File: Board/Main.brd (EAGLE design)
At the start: 40.6 x 45.7 mm, 9 parts, among them M1 LB1909MC, M2 LB1909MC

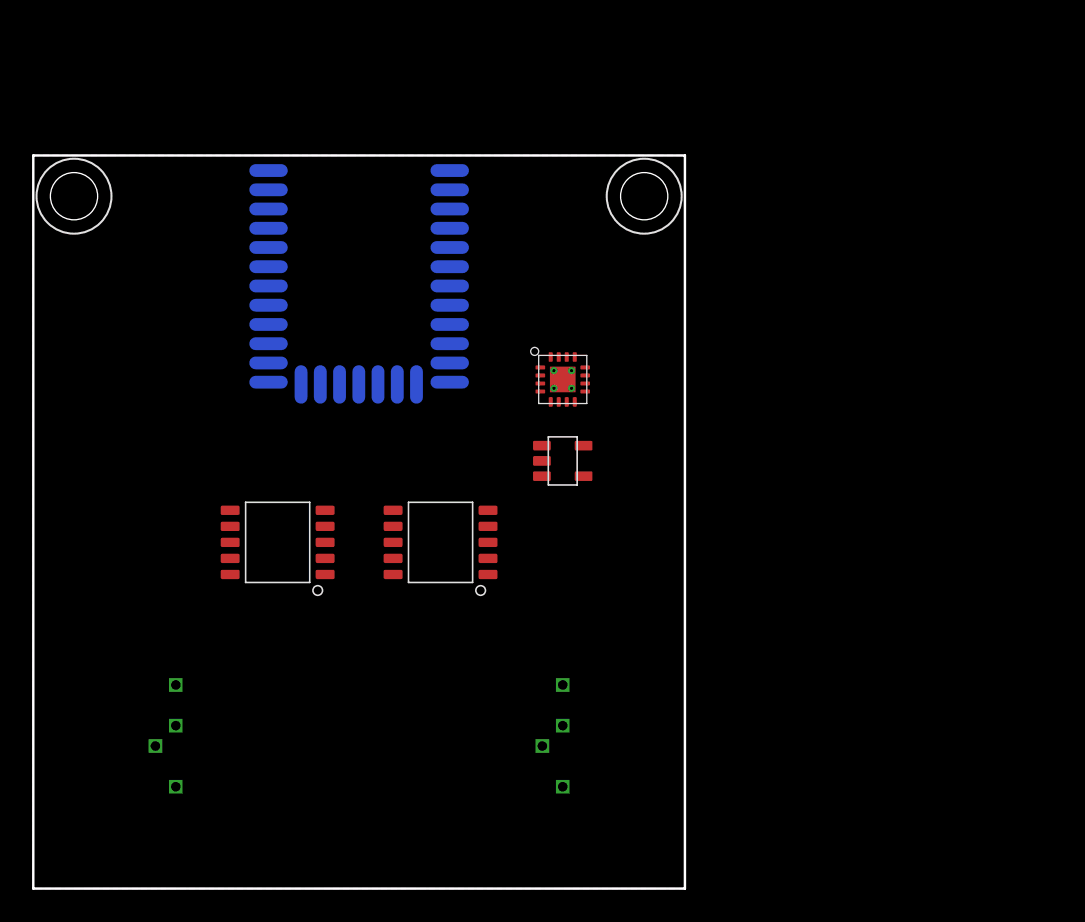
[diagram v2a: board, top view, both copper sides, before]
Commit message: Add USB connector
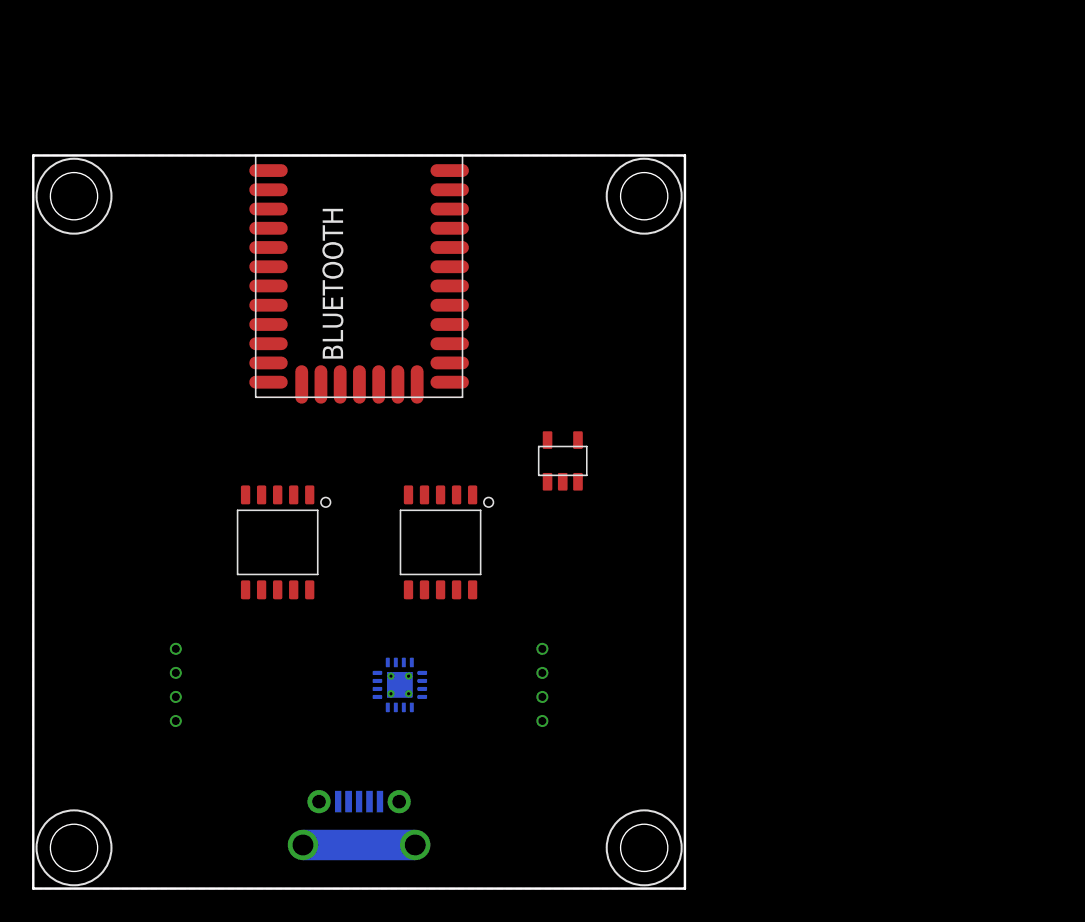
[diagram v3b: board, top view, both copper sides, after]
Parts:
- added LI-PO: 500mAh, Hardware:BATTERY
- added U$5, U$6: (no value), Hardware:#4_SCREW
- added USB: USB, Components:USB
- moved CHARGER 21.6 mm to (2.54, -10.2), flipped to the bottom, turned to 90 degrees
- moved U$3 2.84 mm to (11.4, -10.2), flipped to the bottom
- moved U$4 2.54 mm to (-11.4, -10.2), flipped to the bottom
- flipped BLUETOOTH to the top
- turned M1 to 270 degrees
- turned M2 to 270 degrees
- turned REGULATOR to 90 degrees
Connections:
- net +5V0: now also USB.1
- net GND: now also USB.5, USB.GND@0, USB.GND@1, USB.GND@2, USB.GND@3
- net N$2: now also U$4.B2; no longer U$4.P$2
- net N$3: now also U$3.B2; no longer U$3.P$2
- net N$4: now also U$3.B1; no longer U$3.P$1
- net N$5: now also U$4.B1; no longer U$4.P$1
- net N$6: now also U$4.A1; no longer U$4.P$3
- net N$7: now also U$4.A2; no longer U$4.P$4
- net N$8: now also U$3.A1; no longer U$3.P$3
- net N$9: now also U$3.A2; no longer U$3.P$4
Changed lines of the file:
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@@
 </autorouter>
 <elements>
-<element name="CHARGER" library="Main Components" package="VQFN-16" value="BQ24075" x="12.7" y="8.89" smashed="yes">
-<attribute name="VALUE" value="BQ24075" x="12.7" y="8.89" size="1.778" layer="27" display="off"/>
+<element name="CHARGER" library="Main Components" package="VQFN-16" value="BQ24075" x="2.54" y="-10.16" smashed="yes" rot="MR90">
+<attribute name="VALUE" value="BQ24075" x="2.54" y="-10.16" size="1.778" layer="28" rot="MR90" display="off"/>
 </element>
-<element name="BLUETOOTH" library="Main Components" package="BGM111" value="BGM111" x="0" y="22.86" smashed="yes" rot="MR0">
-<attribute name="NAME" x="1" y="14.86" size="1.27" layer="26" font="vector" rot="MR90" align="bottom-center"/>
-<attribute name="VALUE" x="-2" y="14.86" size="1.27" layer="28" font="vector" rot="MR90" align="bottom-center"/>
+<element name="BLUETOOTH" library="Main Components" package="BGM111" value="BGM111" x="0" y="22.86" smashed="yes">
+<attribute name="NAME" x="-1" y="14.86" size="1.27" layer="25" font="vector" rot="R90" align="bottom-center"/>
+<attribute name="VALUE" x="2" y="14.86" size="1.27" layer="27" font="vector" rot="R90" align="bottom-center"/>
 </element>
 <element name="U$1" library="Hardware" package="#4_SCREW" value="" x="-17.78" y="20.32" smashed="yes"/>
 <element name="U$2" library="Hardware" package="#4_SCREW" value="" x="17.78" y="20.32" smashed="yes"/>
-<element name="REGULATOR" library="Components" package="SOT-23-5" value="TLV755P" x="12.7" y="3.81" smashed="yes"/>
-<element name="M1" library="Components" package="SOIC-10" value="LB1909MC" x="-5.08" y="-1.27" smashed="yes" rot="R180"/>
-<element name="M2" library="Components" package="SOIC-10" value="LB1909MC" x="5.08" y="-1.27" smashed="yes" rot="R180"/>
-<element name="U$3" library="Components" package="MOTOR" value="MOTOR" x="12.7" y="-12.7" smashed="yes" rot="R90"/>
-<element name="U$4" library="Components" package="MOTOR" value="MOTOR" x="-11.43" y="-12.7" smashed="yes" rot="R90"/>
+<element name="REGULATOR" library="Components" package="SOT-23-5" value="TLV755P" x="12.7" y="3.81" smashed="yes" rot="R90"/>
+<element name="M1" library="Components" package="SOIC-10" value="LB1909MC" x="-5.08" y="-1.27" smashed="yes" rot="R270"/>
+<element name="M2" library="Components" package="SOIC-10" value="LB1909MC" x="5.08" y="-1.27" smashed="yes" rot="R270"/>
+<element name="U$3" library="Components" package="MOTOR" value="MOTOR" x="11.43" y="-10.16" smashed="yes" rot="MR90"/>
+<element name="U$4" library="Components" package="MOTOR" value="MOTOR" x="-11.43" y="-10.16" smashed="yes" rot="MR90"/>
+<element name="LI-PO" library="Hardware" package="BATTERY" value="500mAh" x="0" y="6.35" smashed="yes" rot="MR0">
+<attribute name="NAME" x="0" y="7.35" size="2.54" layer="26" font="vector" rot="MR0" align="bottom-center"/>
+<attribute name="VALUE" x="0" y="5.35" size="2.54" layer="28" font="vector" rot="MR0" align="top-center"/>
+</element>
+<element name="USB" library="Components" package="USB" value="USB" x="0" y="-21.59" smashed="yes" rot="MR0"/>
+<element name="U$5" library="Hardware" package="#4_SCREW" value="" x="-17.78" y="-20.32" smashed="yes"/>
+<element name="U$6" library="Hardware" package="#4_SCREW" value="" x="17.78" y="-20.32" smashed="yes"/>
 </elements>
 <signals>
@@
 <contactref element="M1" pad="6"/>
 <contactref element="M2" pad="6"/>
-<wire x1="12.15" y1="8.34" x2="12.7" y2="8.89" width="0" layer="19" extent="1-1"/>
-<wire x1="11.3" y1="8.14" x2="12.15" y2="8.34" width="0" layer="19" extent="1-1"/>
-<wire x1="12.45" y1="10.29" x2="12.15" y2="9.44" width="0" layer="19" extent="1-1"/>
+<contactref element="USB" pad="GND@3"/>
+<contactref element="USB" pad="GND@1"/>
+<contactref element="USB" pad="GND@2"/>
+<contactref element="USB" pad="GND@0"/>
+<contactref element="USB" pad="5"/>
+<wire x1="3.09" y1="-10.71" x2="3.94" y2="-10.41" width="0" layer="19" extent="16-16"/>
+<wire x1="2.54" y1="-10.16" x2="1.99" y2="-10.71" width="0" layer="19" extent="16-16"/>
 </signal>
 <signal name="+3V3">
@@
 <contactref element="M1" pad="1"/>
 <contactref element="M2" pad="1"/>
-<wire x1="8.04" y1="-3.27" x2="14" y2="4.76" width="0" layer="19" extent="1-1"/>
-<wire x1="-2.12" y1="-3.27" x2="8.04" y2="-3.27" width="0" layer="19" extent="1-1"/>
-<wire x1="-5.65" y1="19.52" x2="-2.12" y2="-3.27" width="0" layer="19" extent="1-16"/>
+<wire x1="11.75" y1="5.11" x2="5.65" y2="19.52" width="0" layer="19" extent="1-1"/>
+<wire x1="7.08" y1="1.69" x2="11.75" y2="5.11" width="0" layer="19" extent="1-1"/>
+<wire x1="-3.08" y1="1.69" x2="7.08" y2="1.69" width="0" layer="19" extent="1-1"/>
 </signal>
 <signal name="+5V0">
 <contactref element="CHARGER" pad="13"/>
+<contactref element="USB" pad="1"/>
+<wire x1="3.94" y1="-9.41" x2="1.3" y2="-17.44" width="0" layer="19" extent="16-16"/>
 </signal>
 <signal name="N$1">
@@
 <contactref element="CHARGER" pad="10"/>
 <contactref element="CHARGER" pad="11"/>
-<wire x1="14.1" y1="9.14" x2="14.1" y2="8.64" width="0" layer="19" extent="1-1"/>
-<wire x1="11.4" y1="4.76" x2="14.1" y2="8.64" width="0" layer="19" extent="1-1"/>
-<wire x1="11.4" y1="2.86" x2="11.4" y2="4.76" width="0" layer="19" extent="1-1"/>
+<wire x1="13.65" y1="2.51" x2="11.75" y2="2.51" width="0" layer="19" extent="1-1"/>
+<wire x1="2.29" y1="-8.76" x2="13.65" y2="2.51" width="0" layer="19" extent="1-16"/>
+<wire x1="2.79" y1="-8.76" x2="2.29" y2="-8.76" width="0" layer="19" extent="16-16"/>
 </signal>
 <signal name="N$2">
 <contactref element="M1" pad="7"/>
-<contactref element="U$4" pad="P$2"/>
-<wire x1="-8.04" y1="-0.27" x2="-12.7" y2="-13.97" width="0" layer="19" extent="1-1"/>
+<contactref element="U$4" pad="B2"/>
+<wire x1="-6.08" y1="-4.23" x2="-11.43" y2="-9.41" width="0" layer="19" extent="1-1"/>
 </signal>
 <signal name="N$3">
 <contactref element="M2" pad="7"/>
-<contactref element="U$3" pad="P$2"/>
-<wire x1="2.12" y1="-0.27" x2="11.43" y2="-13.97" width="0" layer="19" extent="1-1"/>
+<contactref element="U$3" pad="B2"/>
+<wire x1="11.43" y1="-9.41" x2="4.08" y2="-4.23" width="0" layer="19" extent="1-1"/>
 </signal>
 <signal name="N$4">
 <contactref element="M2" pad="8"/>
-<contactref element="U$3" pad="P$1"/>
-<wire x1="2.12" y1="-1.27" x2="12.7" y2="-16.51" width="0" layer="19" extent="1-1"/>
+<contactref element="U$3" pad="B1"/>
+<wire x1="5.08" y1="-4.23" x2="11.43" y2="-10.91" width="0" layer="19" extent="1-1"/>
 </signal>
 <signal name="N$5">
 <contactref element="M1" pad="8"/>
-<contactref element="U$4" pad="P$1"/>
-<wire x1="-8.04" y1="-1.27" x2="-11.43" y2="-16.51" width="0" layer="19" extent="1-1"/>
+<contactref element="U$4" pad="B1"/>
+<wire x1="-5.08" y1="-4.23" x2="-11.43" y2="-10.91" width="0" layer="19" extent="1-1"/>
 </signal>
 <signal name="N$6">
-<contactref element="U$4" pad="P$3"/>
+<contactref element="U$4" pad="A1"/>
 <contactref element="M1" pad="9"/>
-<wire x1="-8.04" y1="-2.27" x2="-11.43" y2="-12.7" width="0" layer="19" extent="1-1"/>
+<wire x1="-4.08" y1="-4.23" x2="-11.43" y2="-12.41" width="0" layer="19" extent="1-1"/>
 </signal>
 <signal name="N$7">
 <contactref element="M1" pad="10"/>
-<contactref element="U$4" pad="P$4"/>
-<wire x1="-8.04" y1="-3.27" x2="-11.43" y2="-10.16" width="0" layer="19" extent="1-1"/>
+<contactref element="U$4" pad="A2"/>
+<wire x1="-3.08" y1="-4.23" x2="-11.43" y2="-7.91" width="0" layer="19" extent="1-1"/>
 </signal>
 <signal name="N$8">
 <contactref element="M2" pad="9"/>
-<contactref element="U$3" pad="P$3"/>
-<wire x1="12.7" y1="-12.7" x2="2.12" y2="-2.27" width="0" layer="19" extent="1-1"/>
+<contactref element="U$3" pad="A1"/>
+<wire x1="6.08" y1="-4.23" x2="11.43" y2="-12.41" width="0" layer="19" extent="1-1"/>
 </signal>
 <signal name="N$9">
 <contactref element="M2" pad="10"/>
-<contactref element="U$3" pad="P$4"/>
-<wire x1="12.7" y1="-10.16" x2="2.12" y2="-3.27" width="0" layer="19" extent="1-1"/>
+<contactref element="U$3" pad="A2"/>
+<wire x1="11.43" y1="-7.91" x2="7.08" y2="-4.23" width="0" layer="19" extent="1-1"/>
 </signal>
 </signals>
